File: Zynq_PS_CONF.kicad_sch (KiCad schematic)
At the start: 18 parts, among them U1 XC7Z020-2CLG484I, U5 ASDMB1-33.333MHZ-LY-T

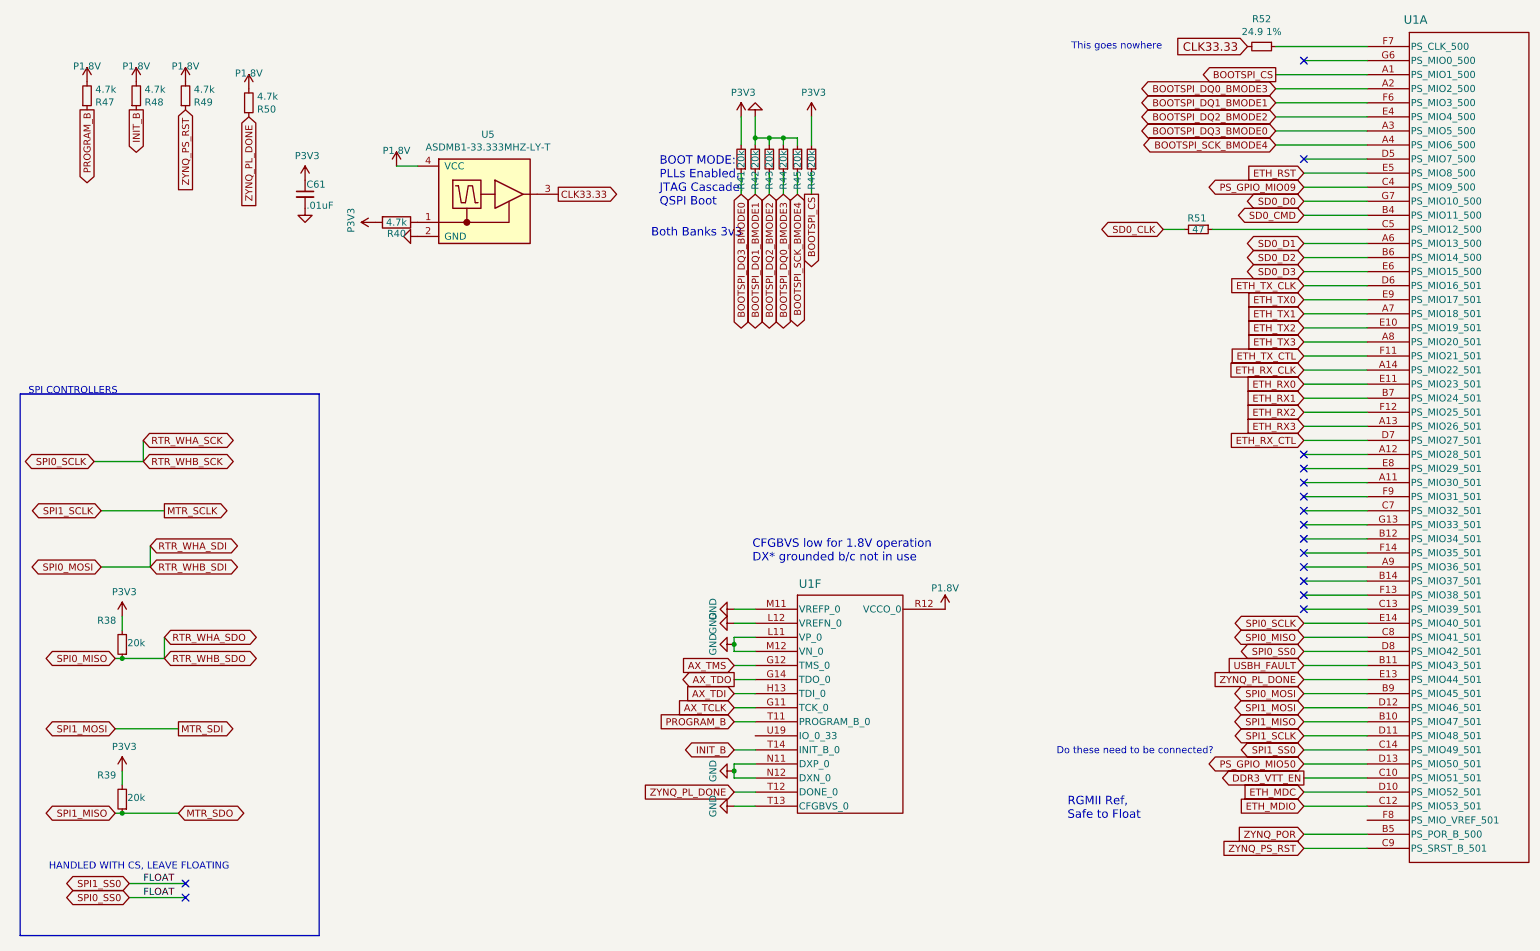
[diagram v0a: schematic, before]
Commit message: updated layouts, added motor
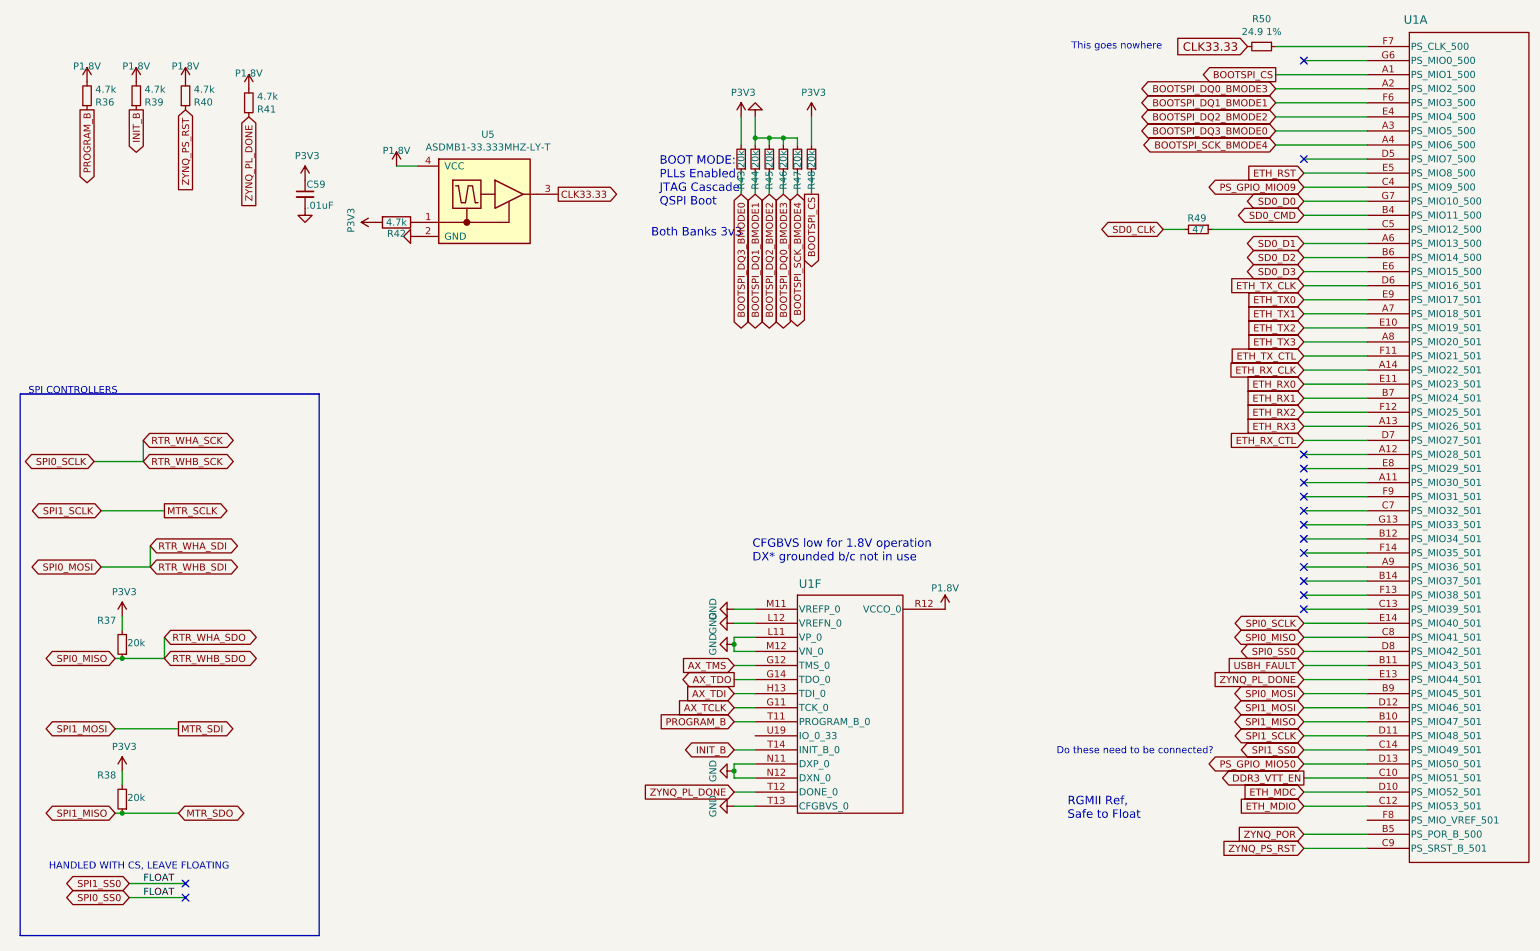
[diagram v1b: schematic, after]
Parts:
- renumbered C61 to C59, R47 to R36, R38 to R37, R39 to R38, R48 to R39, R49 to R40, R50 to R41, R40 to R42, R41 to R43, R42 to R44, R43 to R45, R44 to R46, R45 to R47, R46 to R48, R51 to R49, R52 to R50

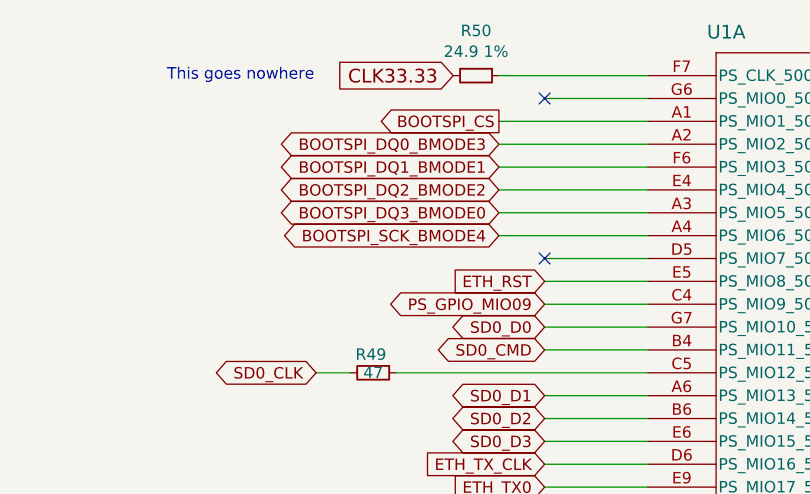
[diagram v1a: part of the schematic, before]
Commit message: SPI feedback repaired
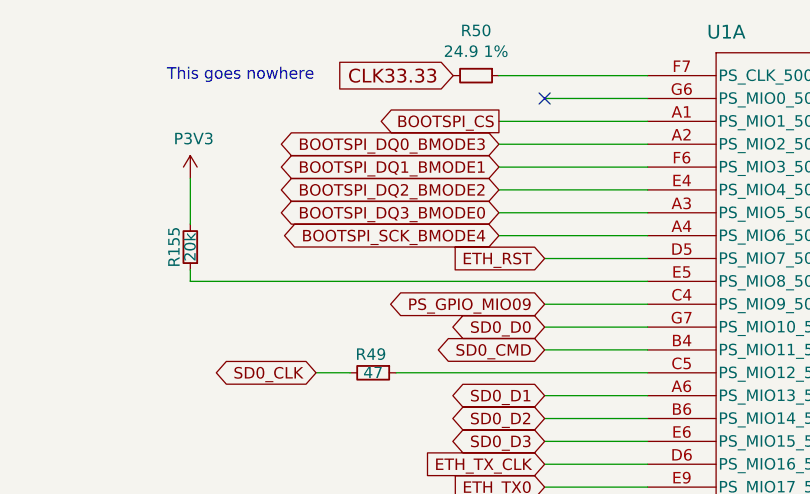
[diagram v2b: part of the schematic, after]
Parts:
- added R155: 20k, Resistor_SMD:R_0402_1005Metric, symbol Device:R_Small
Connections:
- net ETH_RST: now also U1.D5 (PS_MIO7_500); no longer U1.E5 (PS_MIO8_500)
- net P3V3: now also R155.2
- new net: R155.1, U1.E5 (PS_MIO8_500)
- no-connect marks 16 -> 15
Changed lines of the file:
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@@
 	)
 	(no_connect
-		(at 243.84 39.37)
-	)
-	(no_connect
 		(at 41.91 172.72)
 	)
@@
 	(wire
 		(pts
+			(xy 204.47 41.91) (xy 204.47 40.64)
+		)
+		(stroke
+			(width 0)
+			(type default)
+		)
+	)
+	(wire
+		(pts
 			(xy 238.76 31.75) (xy 255.27 31.75)
 		)
@@
 	(wire
 		(pts
+			(xy 204.47 41.91) (xy 255.27 41.91)
+		)
+		(stroke
+			(width 0)
+			(type default)
+		)
+	)
+	(wire
+		(pts
 			(xy 243.84 85.09) (xy 255.27 85.09)
 		)
@@
 	(wire
 		(pts
-			(xy 243.84 41.91) (xy 255.27 41.91)
+			(xy 243.84 21.59) (xy 255.27 21.59)
 		)
 		(stroke
@@
 	(wire
 		(pts
-			(xy 243.84 21.59) (xy 255.27 21.59)
+			(xy 243.84 92.71) (xy 255.27 92.71)
 		)
 		(stroke
@@
 	(wire
 		(pts
-			(xy 243.84 92.71) (xy 255.27 92.71)
+			(xy 204.47 35.56) (xy 204.47 30.48)
 		)
 		(stroke
@@
 		)
 	)
-	(global_label "ETH_RST"
-		(shape input)
-		(at 243.84 41.91 180)
+	(global_label "BOOTSPI_DQ2_BMODE2"
+		(shape bidirectional)
+		(at 147.32 45.72 270)
 		(fields_autoplaced yes)
 		(effects
@@
 		)
 		(property "Intersheetrefs" "${INTERSHEET_REFS}"
-			(at 235.1626 41.91 0)
+			(at 147.32 71.225 90)
 			(show_name no)
 			(do_not_autoplace no)
@@
 		)
 	)
-	(global_label "BOOTSPI_DQ2_BMODE2"
+	(global_label "BOOTSPI_DQ3_BMODE0"
 		(shape bidirectional)
-		(at 147.32 45.72 270)
+		(at 238.76 34.29 180)
 		(fields_autoplaced yes)
 		(effects
@@
 		)
 		(property "Intersheetrefs" "${INTERSHEET_REFS}"
-			(at 147.32 71.225 90)
+			(at 212.0726 34.29 0)
 			(show_name no)
 			(do_not_autoplace no)
@@
 		)
 	)
-	(global_label "BOOTSPI_DQ3_BMODE0"
+	(global_label "PS_GPIO_MIO50"
 		(shape bidirectional)
-		(at 238.76 34.29 180)
+		(at 243.84 148.59 180)
 		(fields_autoplaced yes)
 		(effects
@@
 		)
 		(property "Intersheetrefs" "${INTERSHEET_REFS}"
-			(at 212.0726 34.29 0)
+			(at 227.2011 148.59 0)
 			(show_name no)
 			(do_not_autoplace no)
@@
 		)
 	)
-	(global_label "PS_GPIO_MIO50"
-		(shape bidirectional)
-		(at 243.84 148.59 180)
+	(global_label "ETH_RST"
+		(shape input)
+		(at 243.84 39.37 180)
 		(fields_autoplaced yes)
 		(effects
@@
 		)
 		(property "Intersheetrefs" "${INTERSHEET_REFS}"
-			(at 227.2011 148.59 0)
+			(at 235.1626 39.37 0)
 			(show_name no)
 			(do_not_autoplace no)
@@
 	(symbol
 		(lib_id "power:+3V3")
+		(at 204.47 30.48 0)
+		(unit 1)
+		(body_style 1)
+		(exclude_from_sim no)
+		(in_bom yes)
+		(on_board yes)
+		(in_pos_files yes)
+		(dnp no)
+		(property "Reference" "#PWR0330"
+			(at 204.47 34.29 0)
+			(hide yes)
+			(show_name no)
+			(do_not_autoplace no)
+			(effects
+				(font
+					(size 1.27 1.27)
+				)
+			)
+		)
+		(property "Value" "P3V3"
+			(at 204.851 26.0858 0)
+			(show_name no)
+			(do_not_autoplace no)
+			(effects
+				(font
+					(size 1.27 1.27)
+				)
+			)
+		)
+		(property "Footprint" ""
+			(at 204.47 30.48 0)
+			(hide yes)
+			(show_name no)
+			(do_not_autoplace no)
+			(effects
+				(font
+					(size 1.27 1.27)
+				)
+			)
+		)
+		(property "Datasheet" ""
+			(at 204.47 30.48 0)
+			(hide yes)
+			(show_name no)
+			(do_not_autoplace no)
+			(effects
+				(font
+					(size 1.27 1.27)
+				)
+			)
+		)
+		(property "Description" ""
+			(at 204.47 30.48 0)
+			(show_name no)
+			(do_not_autoplace no)
+			(effects
+				(font
+					(size 1.27 1.27)
+				)
+			)
+		)
+		(pin "1"
+		)
+		(instances
+			(project "Flight_Computer_REV01"
+				(path "/90c8068e-3eef-45e4-910c-02ec589c7ae1/02d20871-377f-47d8-ae1f-b9e257fffeb5"
+					(reference "#PWR0330")
+					(unit 1)
+				)
+			)
+		)
+	)
+	(symbol
+		(lib_id "power:+3V3")
 		(at 30.48 149.86 0)
 		(unit 1)
@@
 					(unit 1)
 				)
+			)
+		)
+	)
+	(symbol
+		(lib_id "Device:R_Small")
+		(at 204.47 38.1 180)
+		(unit 1)
+		(body_style 1)
+		(exclude_from_sim no)
+		(in_bom yes)
+		(on_board yes)
+		(in_pos_files yes)
+		(dnp no)
+		(property "Reference" "R155"
+			(at 202.692 38.1 90)
+			(show_name no)
+			(do_not_autoplace no)
+			(effects
+				(font
+					(size 1.27 1.27)
+				)
+			)
+		)
+		(property "Value" "20k"
+			(at 204.47 38.1 90)
+			(show_name no)
+			(do_not_autoplace no)
+			(effects
+				(font
+					(size 1.27 1.27)
+				)
+			)
+		)
+		(property "Footprint" "Resistor_SMD:R_0402_1005Metric"
+			(at 204.47 38.1 0)
+			(hide yes)
+			(show_name no)
+			(do_not_autoplace no)
+			(effects
+				(font
+					(size 1.27 1.27)
+				)
+			)
+		)
+		(property "Datasheet" ""
+			(at 204.47 38.1 0)
+			(hide yes)
+			(show_name no)
+			(do_not_autoplace no)
+			(effects
+				(font
+					(size 1.27 1.27)
+				)
+			)
+		)
+		(property "Description" ""
+			(at 204.47 38.1 0)
+			(show_name no)
+			(do_not_autoplace no)
+			(effects
+				(font
+					(size 1.27 1.27)
+				)
+			)
+		)
+		(pin "2"
+		)
+		(pin "1"
+		)
+		(instances
+			(project "Flight_Computer_REV01"
+				(path "/90c8068e-3eef-45e4-910c-02ec589c7ae1/02d20871-377f-47d8-ae1f-b9e257fffeb5"
+					(reference "R155")
+					(unit 1)
+				)

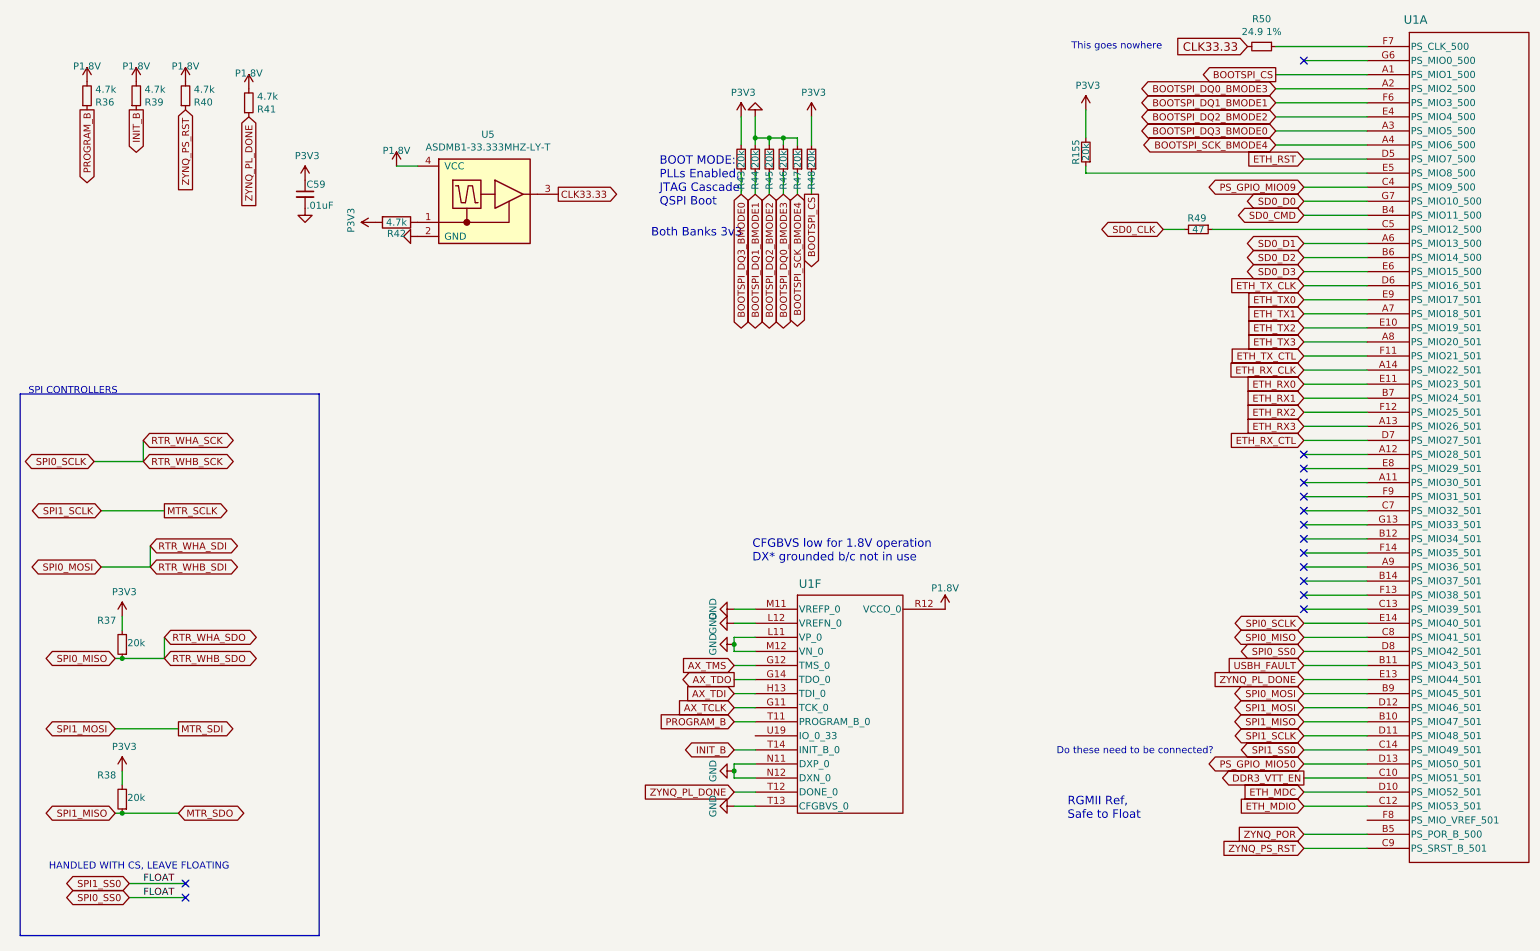
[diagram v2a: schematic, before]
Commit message: Changes to layout pins
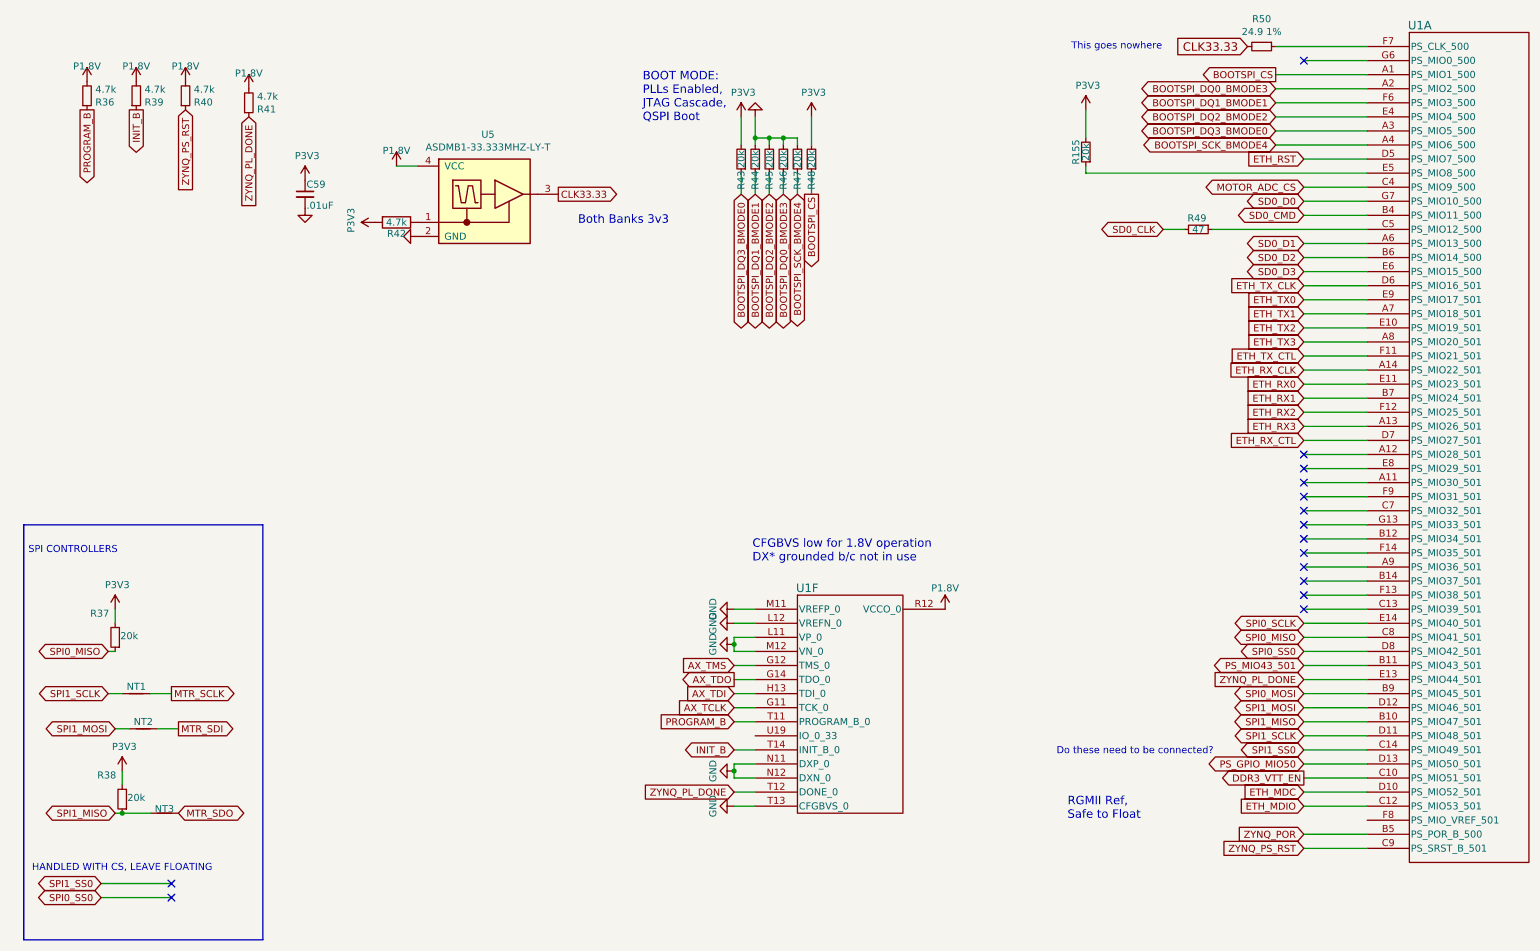
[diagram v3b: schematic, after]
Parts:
- added NT1, NT2, NT3: NetTie_2, symbol Device:NetTie_2
- U1: footprint DFTcustom:BGA-484_19.0x19.0mm_Layout22x22_P0.80mm_dia0.40mm -> FPGA:BGA-484_19.0x19.0mm_Layout22x22_P0.80mm_dia0.40mm
- U5: symbol Abracon:ABRACON-ASDMB -> KiCAD_Library_Cooter:ABRACON-ASDMB
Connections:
- net MTR_SCLK: now also NT1.2; no longer U1.D11 (PS_MIO48_501)
- net MTR_SDI: now also NT2.2; no longer U1.D12 (PS_MIO46_501)
- net MTR_SDO: now also NT3.2; no longer R38.1, U1.B10 (PS_MIO47_501)
- net SPI0_SS0: no longer U1.C14 (PS_MIO49_501)
- net PS_GPIO_MIO09 renamed MOTOR_ADC_CS
- net RTR_WHA_SCK renamed SPI0_SCLK
- net RTR_WHA_SDI renamed SPI0_MOSI
- net RTR_WHA_SDO renamed SPI0_MISO
- net USBH_FAULT renamed PS_MIO43_501
- new net SPI1_MISO: NT3.1, R38.1, U1.B10 (PS_MIO47_501)
- new net SPI1_MOSI: NT2.1, U1.D12 (PS_MIO46_501)
- new net SPI1_SCLK: NT1.1, U1.D11 (PS_MIO48_501)
- new net SPI1_SS0: U1.C14 (PS_MIO49_501)
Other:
- moved on the sheet: R37
